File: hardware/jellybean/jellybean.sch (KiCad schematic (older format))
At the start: 79 parts

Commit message: CPLD JTAG
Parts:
- added P?: CPLD_JTAG, symbol CONN_6
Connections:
- net GND: now also P?.5
- net VCC: now also P?.6
- net CPLD_TDO: now reaches U?.69 (P9_5)
- net CPLD_TDO: now also U?.83 (TDO), P?.3
- net CPLD_TCK: now reaches U?.73 (P6_0)
- net CPLD_TCK: now also U?.48 (TCK), P?.4
- net CPLD_TMS: now reaches U?.74 (P6_1)
- net CPLD_TMS: now also U?.47 (TMS), P?.1
- net CPLD_TDI: now reaches U?.78 (P6_2)
- net CPLD_TDI: now also U?.45 (TDI), P?.2
- no-connect marks 28 -> 27
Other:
- note added: "bank 2 power selection"
- moved on the sheet: C?, K?, R?

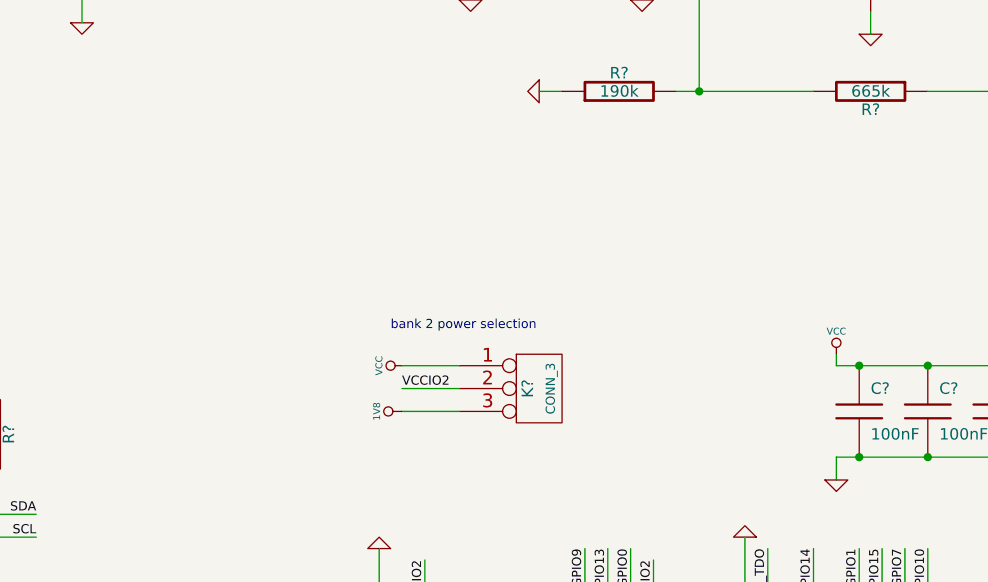
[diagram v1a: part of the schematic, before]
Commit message: power headers
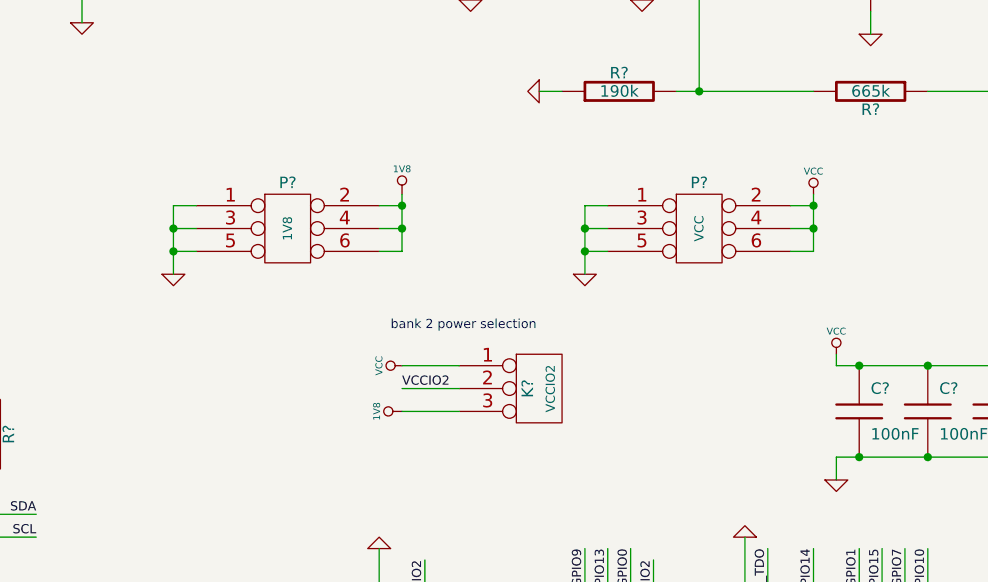
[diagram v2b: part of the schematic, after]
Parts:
- added P?: VCC, symbol CONN_3X2
- added P?: 1V8, symbol CONN_3X2
- K?: value CONN_3 -> VCCIO2
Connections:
- net +1.8V: now also P?.2, P?.4, P?.6
- net GND: now also P?.1, P?.1, P?.3, P?.3, P?.5, P?.5
- net VCC: now also P?.2, P?.4, P?.6
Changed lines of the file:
@@
-EESchema Schematic File Version 2  date Mon Apr  9 10:36:38 2012
+EESchema Schematic File Version 2  date Mon Apr  9 15:57:28 2012
 LIBS:power
 LIBS:device
@@
 Comment4 ""
 $EndDescr
-Text Label 8450 7750 1    40   ~ 0
-CPLD_TDO
+Connection ~ 12500 3150
+Wire Wire Line
+	12400 3150 12500 3150
+Wire Wire Line
+	12400 3350 12500 3350
+Wire Wire Line
+	12500 3350 12500 3100
+Connection ~ 11500 3350
+Wire Wire Line
+	11600 3350 11500 3350
+Connection ~ 14300 3150
+Wire Wire Line
+	14200 3150 14300 3150
+Wire Wire Line
+	14200 3350 14300 3350
+Wire Wire Line
+	14300 3350 14300 3100
+Connection ~ 13300 3250
+Wire Wire Line
+	13400 3250 13300 3250
 Wire Wire Line
 	8450 7450 8450 7750
@@
 Wire Wire Line
 	9700 6500 10000 6500
+Wire Wire Line
+	13300 3450 13300 3150
+Wire Wire Line
+	13300 3150 13400 3150
+Wire Wire Line
+	13400 3350 13300 3350
+Connection ~ 13300 3350
+Wire Wire Line
+	14300 3250 14200 3250
+Connection ~ 14300 3250
+Wire Wire Line
+	11600 3150 11500 3150
+Wire Wire Line
+	11500 3150 11500 3450
+Wire Wire Line
+	11600 3250 11500 3250
+Connection ~ 11500 3250
+Wire Wire Line
+	12400 3250 12500 3250
+Connection ~ 12500 3250
+$Comp
+L 1V8 #PWR?
+U 1 1 4F835A68
+P 12500 3100
+F 0 "#PWR?" H 12500 3240 20  0001 C CNN
+F 1 "1V8" H 12500 3210 30  0000 C CNN
+	1    12500 3100
+	1    0    0    -1
+$EndComp
+$Comp
+L GND #PWR?
+U 1 1 4F835A62
+P 11500 3450
+F 0 "#PWR?" H 11500 3450 30  0001 C CNN
+F 1 "GND" H 11500 3380 30  0001 C CNN
+	1    11500 3450
+	1    0    0    -1
+$EndComp
+$Comp
+L VCC #PWR?
+U 1 1 4F835A55
+P 14300 3100
+F 0 "#PWR?" H 14300 3200 30  0001 C CNN
+F 1 "VCC" H 14300 3200 30  0000 C CNN
+	1    14300 3100
+	1    0    0    -1
+$EndComp
+$Comp
+L GND #PWR?
+U 1 1 4F835A49
+P 13300 3450
+F 0 "#PWR?" H 13300 3450 30  0001 C CNN
+F 1 "GND" H 13300 3380 30  0001 C CNN
+	1    13300 3450
+	1    0    0    -1
+$EndComp
+$Comp
+L CONN_3X2 P?
+U 1 1 4F835A39
+P 12000 3300
+F 0 "P?" H 12000 3550 50  0000 C CNN
+F 1 "1V8" V 12000 3350 40  0000 C CNN
+	1    12000 3300
+	1    0    0    -1
+$EndComp
+$Comp
+L CONN_3X2 P?
+U 1 1 4F835A31
+P 13800 3300
+F 0 "P?" H 13800 3550 50  0000 C CNN
+F 1 "VCC" V 13800 3350 40  0000 C CNN
+	1    13800 3300
+	1    0    0    -1
+$EndComp
+Text Label 8450 7750 1    40   ~ 0
+CPLD_TDO
 Text Label 10000 6500 2    40   ~ 0
 CPLD_TCK
@@
 P 13100 3950
 F 0 "K?" V 13050 3950 50  0000 C CNN
-F 1 "CONN_3" V 13150 3950 40  0000 C CNN
+F 1 "VCCIO2" V 13150 3950 40  0000 C CNN
 	1    13100 3950
 	1    0    0    -1

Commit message: connectors for cables extending to lemondrop
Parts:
- added C?: 47pF, symbol C
- added P?: SPI, symbol CONN_3X2
- added P?: XCVR_CTL, symbol CONN_8X2
- added P?: CLOCK_CTL, symbol CONN_6X2
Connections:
- net EN1V8: now also R?.1; no longer R?.2
- net GCK1: now also P?.9
- net GCK2: now also P?.11
- net GND: now also R?.2, C?.1; no longer R?.1
- net SCL: now also P?.3 (P3)
- net SDA: now also P?.5 (P5)
- net SSP1_MISO: now also P?.6
- net SSP1_MOSI: now also P?.4
- net SSP1_SCK: now also P?.2
- net SSP1_SSEL: now also P?.3
- net XTAL1: now also C?.2, C?.2; no longer C?.1
- net RXHP: now reaches U?.1 (P4_0)
- net RXHP: now also P?.16
- net RXENABLE: now reaches U?.10 (P4_5)
- net RXENABLE: now also P?.13
- net XCVR_EN: now reaches U?.11 (P4_6)
- net XCVR_EN: now also P?.12
- net B1: now reaches U?.37 (P5_0)
- net B1: now also P?.3
- net B2: now reaches U?.39 (P5_1)
- net B2: now also P?.4
- net B3: now reaches U?.46 (P5_2)
- net B3: now also P?.5
- net B4: now reaches U?.54 (P5_3)
- net B4: now also P?.6
- net B5: now reaches U?.57 (P5_4)
- net B5: now also P?.7
- net B6: now reaches U?.58 (P5_5)
- net B6: now also P?.8
- net B7: now reaches U?.63 (P5_6)
- net B7: now also P?.9
- net at U?.65 (P5_7): now also P?.5
- net TXENABLE: now reaches U?.9 (P4_4)
- net TXENABLE: now also P?.15
- net ADC0_0 renamed RSSI
- net RSSI: now also P?.10
- new net INTR: P?.7 (P7)
- new net LPC_CLK: C?.1, P?.6 (P6)
- new net OEB: P?.4 (P4)
- no-connect marks 27 -> 29
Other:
- note added: "CS_AD"
- note added: "CS_XCVR"
- moved on the sheet: C?, R?

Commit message: CPLD AUX headers
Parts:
- added P?: BANK1_AUX, symbol CONN_8X2
- added P?: CONN_16X2, symbol CONN_16X2
- K?: value VCCIO2 -> BANK2_PWR
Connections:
- net GND: now also P?.1, P?.10 (P10), P?.11, P?.12 (P12), P?.13, P?.14 (P14), P?.15, P?.16 (P16), P?.18 (P18), P?.2 (P2), P?.20 (P20), P?.22 (P22), P?.24 (P24), P?.26 (P26), P?.28 (P28), P?.3, P?.30 (P30), P?.32 (P32), P?.4 (P4), P?.5, P?.6 (P6), P?.7, P?.8 (P8), P?.9
- net B2AUX12: now reaches U?.1 (BANK2F1M12)
- net B2AUX12: now also P?.23 (P23)
- net B2AUX4: now reaches U?.10 (BANK2F1M4)
- net B2AUX4: now also P?.7 (P7)
- net B2AUX3: now reaches U?.11 (BANK2F1M3)
- net B2AUX3: now also P?.5 (P5)
- net B2AUX2: now reaches U?.12 (BANK2F1M2)
- net B2AUX2: now also P?.3 (P3)
- net B2AUX1: now reaches U?.13 (BANK2F1M1)
- net B2AUX1: now also P?.1 (P1)
- net B2AUX11: now reaches U?.2 (BANK2F1M11)
- net B2AUX11: now also P?.21 (P21)
- net B2AUX10: now reaches U?.3 (BANK2F1M10)
- net B2AUX10: now also P?.19 (P19)
- net B2AUX9: now reaches U?.4 (BANK2F1M9)
- net B2AUX9: now also P?.17 (P17)
- net B1AUX9: now reaches U?.49 (BANK1F4M9)
- net B1AUX9: now also P?.2
- net B1AUX10: now reaches U?.50 (BANK1F4M10)
- net B1AUX10: now also P?.4
- net B1AUX11: now reaches U?.52 (BANK1F4M11)
- net B1AUX11: now also P?.6
- net B1AUX12: now reaches U?.53 (BANK1F4M12)
- net B1AUX12: now also P?.8
- net B1AUX13: now reaches U?.55 (BANK1F4M13)
- net B1AUX13: now also P?.10
- net B1AUX14: now reaches U?.56 (BANK1F4M14)
- net B1AUX14: now also P?.12
- net B1AUX15: now reaches U?.58 (BANK1F4M15)
- net B1AUX15: now also P?.14
- net B2AUX8: now reaches U?.6 (BANK2F1M8)
- net B2AUX8: now also P?.15 (P15)
- net B1AUX16: now reaches U?.60 (BANK1F4M16)
- net B1AUX16: now also P?.16
- net B2AUX7: now reaches U?.7 (BANK2F1M7)
- net B2AUX7: now also P?.13 (P13)
- net B2AUX6: now reaches U?.8 (BANK2F1M6)
- net B2AUX6: now also P?.11 (P11)
- net B2AUX5: now reaches U?.9 (BANK2F1M5)
- net B2AUX5: now also P?.9 (P9)
- net B2AUX16: now reaches U?.92 (BANK2F1M16)
- net B2AUX16: now also P?.31 (P31)
- net B2AUX15: now reaches U?.94 (BANK2F1M15)
- net B2AUX15: now also P?.29 (P29)
- net B2AUX14: now reaches U?.97 (BANK2F1M14)
- net B2AUX14: now also P?.27 (P27)
- net B2AUX13: now reaches U?.99 (BANK2F1M13)
- net B2AUX13: now also P?.25
- no-connect marks 29 -> 32
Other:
- moved on the sheet: C?, P?

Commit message: LPC AUX headers
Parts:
- added P?: SD, symbol CONN_6X2
- added P?: GPIO, symbol CONN_8X2
- added P?: ANALOG, symbol CONN_4X2
- added P?: LPC_AUX, symbol CONN_12X2
- P?: value CONN_6X2 -> SPIFI
- P?: value CONN_16X2 -> BANK2_AUX
- R?: value 12k 1% -> 12k
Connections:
- net ADC0_1 is gone; now on net RSSI: U?.2 (ADC0_1/ADC1_1)
- net CTIN_2: now also P?.13 (P13)
- net CTIN_4: now also P?.1 (P1)
- net CTIN_6: now also P?.23 (P23)
- net CTIN_7: now also P?.11 (P11)
- net CTOUT_2: now also P?.7 (P7)
- net CTOUT_4: now also P?.3 (P3)
- net CTOUT_5: now also P?.5 (P5)
- net CTOUT_6: now also P?.21 (P21)
- net CTOUT_7: now also P?.9 (P9)
- net GND: now also P?.1, P?.1, P?.1 (P1), P?.10 (P10), P?.11, P?.12 (P12), P?.13, P?.14 (P14), P?.15, P?.16 (P16), P?.18 (P18), P?.2 (P2), P?.20 (P20), P?.22 (P22), P?.24 (P24), P?.3, P?.3, P?.4 (P4), P?.5, P?.5, P?.6 (P6), P?.7, P?.7, P?.8 (P8), P?.9
- net RSSI: no longer U?.6 (ADC0_0/ADC1_0/DAC)
- net SD_CD: now also P?.3 (P3)
- net SD_CLK: now also P?.11
- net SD_CMD: now also P?.9
- net SD_DAT0: now also P?.7 (P7)
- net SD_DAT1: now also P?.6 (P6)
- net SD_DAT2: now also P?.5 (P5)
- net SD_DAT3: now also P?.4 (P4)
- net SD_POW: now also P?.10
- net SD_VOLT0: now also P?.8 (P8)
- net U3_RXD: now also P?.15 (P15)
- net U3_TXD: now also P?.17 (P17)
- net VCC: now also P?.2 (P2)
- net GPIO3_9: now reaches U?.113 (P7_1)
- net GPIO3_9: now also P?.4
- net GPIO3_10: now reaches U?.115 (P7_2)
- net GPIO3_10: now also P?.6
- net ADC0_6: now reaches U?.142 (ADC0_6/ADC1_6)
- net ADC0_6: now also P?.2
- net ADC0_2: now reaches U?.143 (ADC0_2/ADC1_2)
- net ADC0_2: now also P?.4
- net ADC0_5: now reaches U?.144 (ADC0_5/ADC1_5)
- net ADC0_5: now also P?.6
- net T2_MAT0: now reaches U?.85 (P6_7)
- net T2_MAT0: now also P?.19 (P19)
- net CTIN_3 renamed GPIO3_11
- net GPIO3_11: now also P?.8
- net CTOUT_0: no longer names the net of U?.8 (P4_2)
- net CTOUT_1: no longer names the net of U?.3 (P4_1)
- net CTOUT_14 renamed GPIO3_8
- net GPIO3_8: now also P?.2
- net CTOUT_15: no longer names the net of U?.112 (P3_0)
- net TRACEDATA[0] renamed GPIO3_12
- net GPIO3_12: now also P?.10
- net TRACEDATA[1] renamed GPIO3_13
- net GPIO3_13: now also P?.12
- net TRACEDATA[2] renamed GPIO3_14
- net GPIO3_14: now also P?.14
- net TRACEDATA[3] renamed GPIO3_15
- net GPIO3_15: now also P?.16
- net TRST: no longer names the net of U?.29 (TRST)
- new net ADC0_0: P?.8, U?.6 (ADC0_0/ADC1_0/DAC)
- no-connect marks 32 -> 37
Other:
- note added: "1%"
- moved on the sheet: C?, P?, R?

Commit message: LPC AUX header improvement
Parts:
- removed P?: LPC_AUX, symbol CONN_12X2
- added P?: LPC_AUX, symbol CONN_16X2
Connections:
- net T2_MAT0 is gone; now on net OEB: U?.85 (P6_7)
- net CTIN_2: now also P?.13 (P13)
- net CTIN_4: now also P?.1 (P1)
- net CTIN_6: now also P?.21 (P21)
- net CTIN_7: now also P?.11 (P11)
- net CTOUT_2: now also P?.7 (P7)
- net CTOUT_4: now also P?.3 (P3)
- net CTOUT_5: now also P?.5 (P5)
- net CTOUT_6: now also P?.19 (P19)
- net CTOUT_7: now also P?.9 (P9)
- net DBGEN: now also P?.27 (P27)
- net GND: now also P?.10 (P10), P?.12 (P12), P?.14 (P14), P?.16 (P16), P?.18 (P18), P?.2 (P2), P?.20 (P20), P?.22 (P22), P?.24 (P24), P?.26 (P26), P?.28 (P28), P?.30 (P30), P?.32 (P32), P?.4 (P4), P?.6 (P6), P?.8 (P8)
- net INTR: now also U?.86 (P6_8)
- net TRACECLK: now also P?.23 (P23)
- net U3_RXD: now also P?.15 (P15)
- net U3_TXD: now also P?.17 (P17)
- net VCC: now also P?.31 (P31)
- net WAKEUP: now also P?.25
- net TRST: now reaches U?.29 (TRST)
- net TRST: now also P?.29 (P29)
- no-connect marks 37 -> 35
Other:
- moved on the sheet: P?

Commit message: ESD protect USB ID pin
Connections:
- net DM: now also U?.3 (ESD2); no longer U?.6 (ESD4)
- net DP: now also U?.1 (ESD1); no longer U?.4 (ESD3)
- net ID: now also U?.6 (ESD4)
- net VBUS: no longer C?.1, C?.1, U?.5 (VP)
- net at FB?.1, J?.1 (VBUS): now also C?.1, C?.1, U?.5 (VP)
- no-connect marks 35 -> 34
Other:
- moved on the sheet: C?, FB?, P?, U?
